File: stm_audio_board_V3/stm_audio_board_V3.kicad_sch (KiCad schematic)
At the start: 0 parts

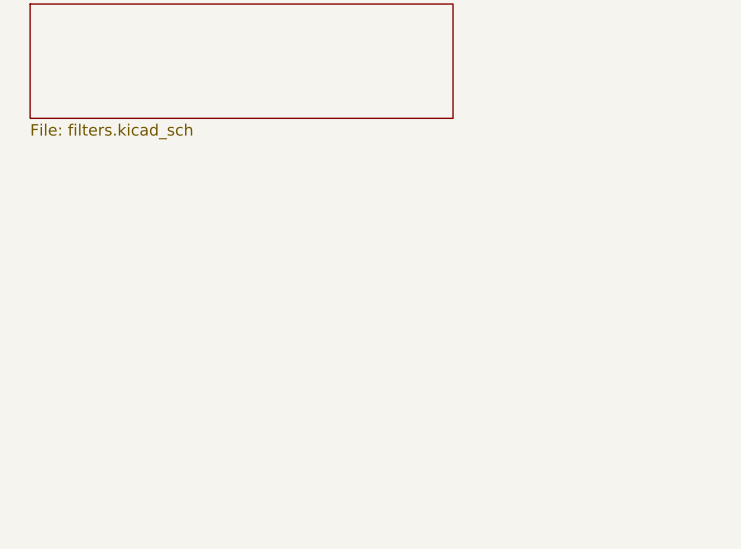
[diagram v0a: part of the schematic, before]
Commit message: Input and output stages are made and assembly started on pcb view
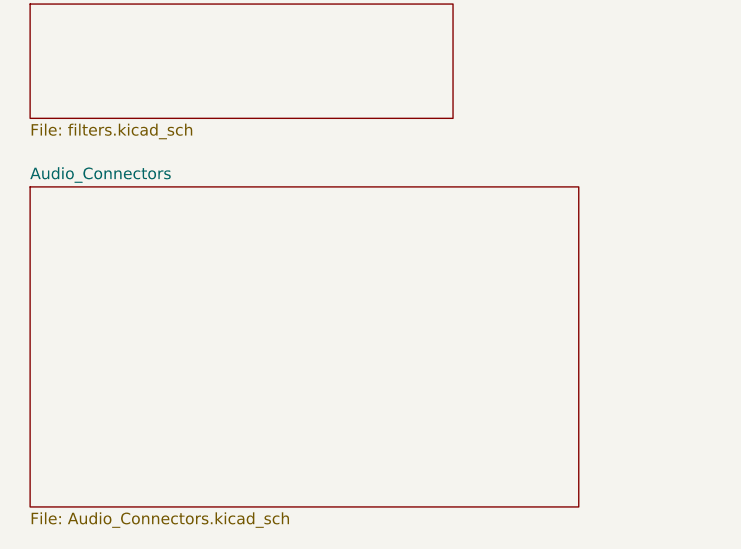
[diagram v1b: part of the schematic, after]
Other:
- added sheet Audio_Connectors (Audio_Connectors.kicad_sch)
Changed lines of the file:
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@@
 (kicad_sch (version 20230121) (generator eeschema)
-  (paper "A4")
+  (paper "A3")
   (sheet (at 21.59 36.83) (size 57.15 22.86) (fields_autoplaced)
     (stroke (width 0.1524) (type solid))
@@
       )
     )
+  )
+  (sheet (at 22.86 198.12) (size 60.96 35.56) (fields_autoplaced)
+    (stroke (width 0.1524) (type solid))
+    (fill (color 0 0 0 0.0000))
+    (property "Sheetname" "Audio_Connectors" (at 22.86 197.4084 0)
+      (effects (font (size 1.27 1.27)) (justify left bottom))
+    )
+    (property "Sheetfile" "Audio_Connectors.kicad_sch" (at 22.86 234.2646 0)
+      (effects (font (size 1.27 1.27)) (justify left top))
+    )
+    (instances
+      (project "stm_audio_board_V3"
+        (path "/6997cf63-2615-4e49-9471-e7da1b6bae71" (page "13"))
+      )
+    )
